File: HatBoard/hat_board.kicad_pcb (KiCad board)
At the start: 4 copper layers, 144 x 78 mm, 108 parts, among them J1 Molex FC Connection, J11 Molex FC Connection, J12 DF11 FC Connection, J17 Molex FC Connection, J18 DF11 FC Connection, J2 DF11 FC Connection, J23 Molex FC Connection, J24 DF11 FC Connection, J29 Molex FC Connection, J30 DF11 FC Connection, J35 Molex FC Connection, J36 DF11 FC Connection, SW1 SW_SPDT_321, SW2 SW_SPDT_321, SW3 SW_SPDT_321, SW4 SW_SPDT_321, SW5 SW_SPDT_321, SW6 SW_SPDT_321, U1 VEML7700, U10 VEML7700, U11 MCP9808_DFN, U12 DRV2605LDGS, U13 TCA4311A, U14 VEML7700, U15 MCP9808_DFN, U16 DRV2605LDGS, U17 TCA4311A, U18 VEML7700, U19 MCP9808_DFN, U2 DRV2605LDGS, U20 DRV2605LDGS, U21 TCA4311A, U22 VEML7700, U23 MCP9808_DFN, U24 DRV2605LDGS, U3 MCP9808_DFN, U4 TCA4311A, U5 TCA4311A, U6 VEML7700, U7 MCP9808_DFN, U8 DRV2605LDGS, U9 TCA4311A

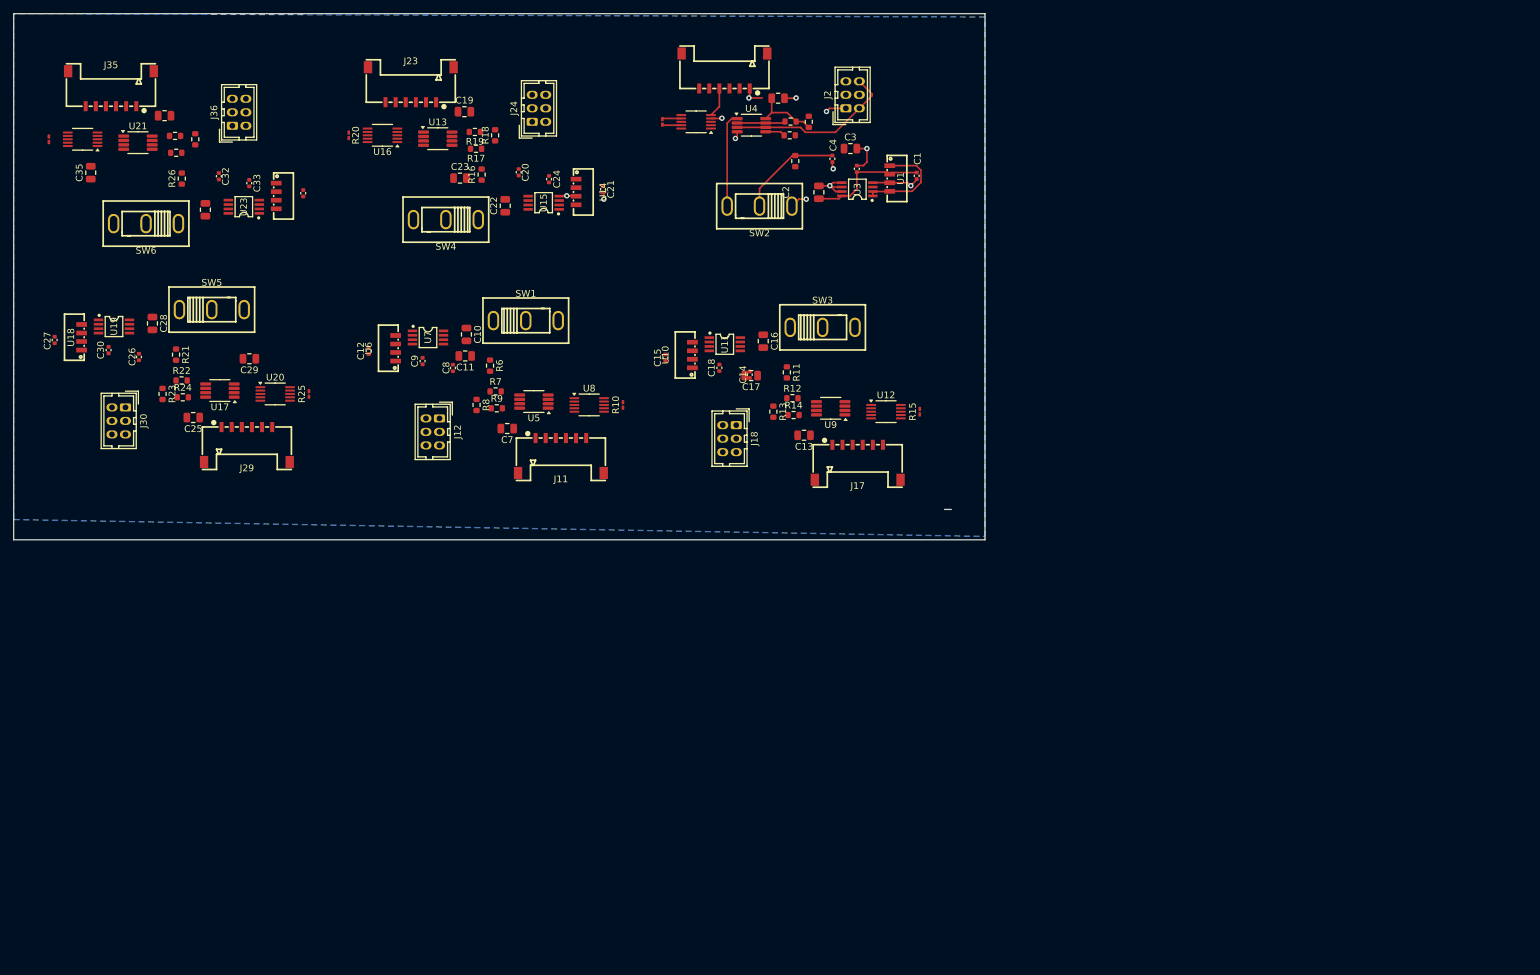
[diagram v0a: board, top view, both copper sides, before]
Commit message: placement with new temp sensor
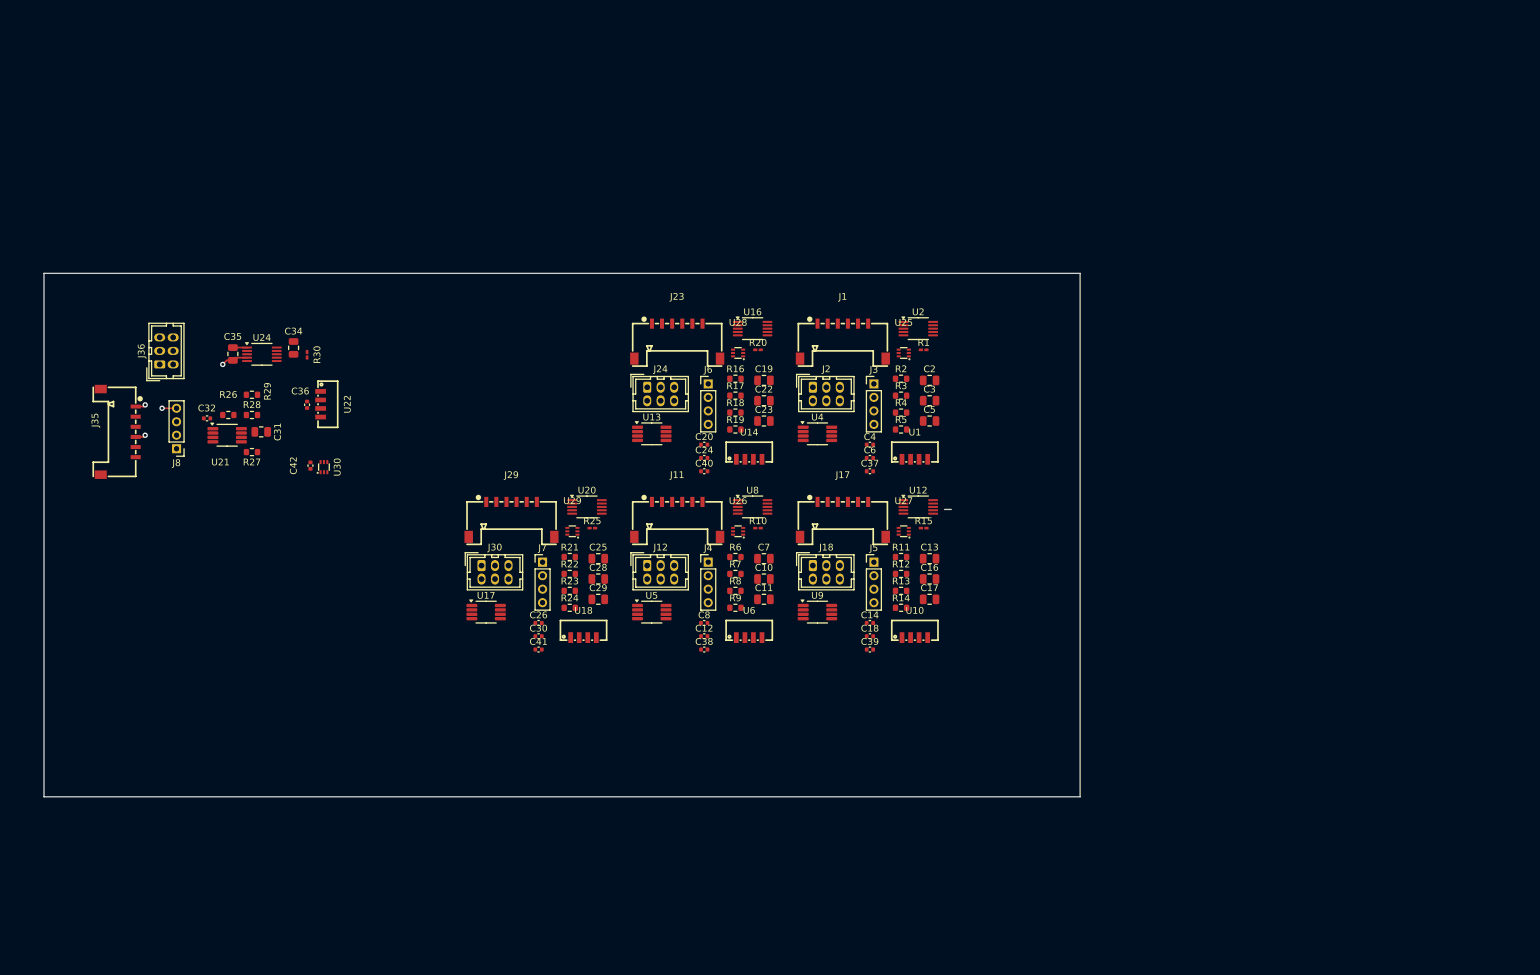
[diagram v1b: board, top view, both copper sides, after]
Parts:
- removed C1, C15, C21, C27, C33, C9: 100nF, Capacitor_SMD:C_0402_1005Metric
- removed SW1, SW2, SW3, SW4, SW5, SW6: SW_SPDT_321, easyeda2kicad:SW-TH_3P-P4.80-HX-SS12D10G4
- removed U11, U15, U19, U23, U3, U7: MCP9808_DFN, easyeda2kicad:MSOP-8_L3.0-W3.0-P0.65-LS4.9-BL
- added C37: 10nF, Capacitor_SMD:C_0402_1005Metric, F.Cu at (159.4, 93.8)
- added C38: 10nF, Capacitor_SMD:C_0402_1005Metric, F.Cu at (134.9, 120.3)
- added C39: 10nF, Capacitor_SMD:C_0402_1005Metric, F.Cu at (159.4, 120.3)
- added C40: 10nF, Capacitor_SMD:C_0402_1005Metric, F.Cu at (134.9, 93.8)
- added C41: 10nF, Capacitor_SMD:C_0402_1005Metric, F.Cu at (110.3, 120.3)
- added C42: 10nF, Capacitor_SMD:C_0402_1005Metric, F.Cu at (76.5, 93.0)
- added J3: Conn_01x04, Connector_PinHeader_2.00mm:PinHeader_1x04_P2.00mm_Vertical, F.Cu at (160.0, 80.9)
- added J4: Conn_01x04, Connector_PinHeader_2.00mm:PinHeader_1x04_P2.00mm_Vertical, F.Cu at (135.5, 107.3)
- added J5: Conn_01x04, Connector_PinHeader_2.00mm:PinHeader_1x04_P2.00mm_Vertical, F.Cu at (160.0, 107.3)
- added J6: Conn_01x04, Connector_PinHeader_2.00mm:PinHeader_1x04_P2.00mm_Vertical, F.Cu at (135.5, 80.9)
- added J7: Conn_01x04, Connector_PinHeader_2.00mm:PinHeader_1x04_P2.00mm_Vertical, F.Cu at (110.9, 107.3)
- added J8: Conn_01x04, Connector_PinHeader_2.00mm:PinHeader_1x04_P2.00mm_Vertical, F.Cu at (56.6, 90.5)
- added U25: TMP112AIDRLR, easyeda2kicad:SOT-563_L1.6-W1.2-P0.50-LS1.6-BR, F.Cu at (164.5, 76.3)
- added U26: TMP112AIDRLR, easyeda2kicad:SOT-563_L1.6-W1.2-P0.50-LS1.6-BR, F.Cu at (139.9, 102.7)
- added U27: TMP112AIDRLR, easyeda2kicad:SOT-563_L1.6-W1.2-P0.50-LS1.6-BR, F.Cu at (164.5, 102.7)
- added U28: TMP112AIDRLR, easyeda2kicad:SOT-563_L1.6-W1.2-P0.50-LS1.6-BR, F.Cu at (139.9, 76.3)
- added U29: TMP112AIDRLR, easyeda2kicad:SOT-563_L1.6-W1.2-P0.50-LS1.6-BR, F.Cu at (115.3, 102.7)
- added U30: TMP112AIDRLR, easyeda2kicad:SOT-563_L1.6-W1.2-P0.50-LS1.6-BR, F.Cu at (78.5, 93.2)
- moved U18 86.7 mm to (117.0, 118.5), turned to 0 degrees
- moved C30 76.6 mm to (110.3, 118.3), turned to 0 degrees
- moved C28 76.2 mm to (119.2, 109.8), turned to 0 degrees
- moved C26 71.2 mm to (110.3, 116.3), turned to 0 degrees
- moved R20 68.5 mm to (142.8, 75.8), turned to 0 degrees
- moved U6 67.7 mm to (141.5, 118.5), turned to 0 degrees
- moved R23 67.1 mm to (114.9, 111.6), turned to 0 degrees
- moved R21 65.6 mm to (114.9, 106.5), turned to 0 degrees
- moved R24 65.3 mm to (114.9, 114.1)
- moved C12 65.3 mm to (134.9, 118.3), turned to 0 degrees
- moved R22 64.3 mm to (114.9, 109.1)
- moved C25 63.6 mm to (119.2, 106.8), turned to 0 degrees
- moved C29 62.8 mm to (119.2, 112.8), turned to 0 degrees
- moved U16 61.9 mm to (142.1, 72.7), turned to 0 degrees
- moved C19 59.7 mm to (143.7, 80.4)
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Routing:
- net GND: track 34.9 -> 7.68 mm, vias 12 -> 3
- net /Face Board/SCLIN: track 25.4 -> 0.00 mm
- net /Face Board/SCL: track 22.2 -> 0.00 mm
- net +3V3: track 22.3 -> 1.51 mm, vias 0 -> 1
- net Net-(SW2-B): track 15.4 -> 0.00 mm
- net Net-(SW2-A): track 14.1 -> 0.00 mm
- net Net-(U4-VCC): track 9.80 -> 0.00 mm
- net Net-(U4-READY): track 2.95 -> 0.00 mm
- net Net-(U2-OUT+): track 2.84 -> 0.00 mm
- net Net-(U2-OUT-): track 2.84 -> 0.00 mm
- net Net-(U24-REG): track 0.00 -> 2.10 mm
- added copper zone on In2.Cu, net +3V3
- added copper zone on In1.Cu, net GND
- removed copper zone on B.Cu, net GND
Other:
- board size 144 x 78 mm -> 153.6 x 77.6 mm

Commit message: finished connections one board, review before copy and clean?
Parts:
- moved J36 4.91 mm to (57.0, 74.0), turned to -90 degrees
- moved R29 1.01 mm to (67.7, 83.5)
- moved C36 0.50 mm to (75.5, 84.0)
- moved C42 0.50 mm to (77.0, 93.0)
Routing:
- net /Face Board5/SCL: track 0.00 -> 42.7 mm, vias 0 -> 1
- net /Face Board5/SCLIN: track 0.00 -> 32.6 mm, vias 0 -> 2
- net GND: track 7.68 -> 26.6 mm, vias 3 -> 14
- net Net-(U21-VCC): track 0.00 -> 12.4 mm, vias 0 -> 2
- net +3V3: track 1.51 -> 13.2 mm, vias 1 -> 9
- net Net-(U24-OUT-): track 0.00 -> 4.84 mm
- net Net-(U24-OUT+): track 0.00 -> 4.78 mm
- net Net-(U21-EN): track 0.00 -> 3.74 mm
- net Net-(U21-READY): track 0.00 -> 1.83 mm

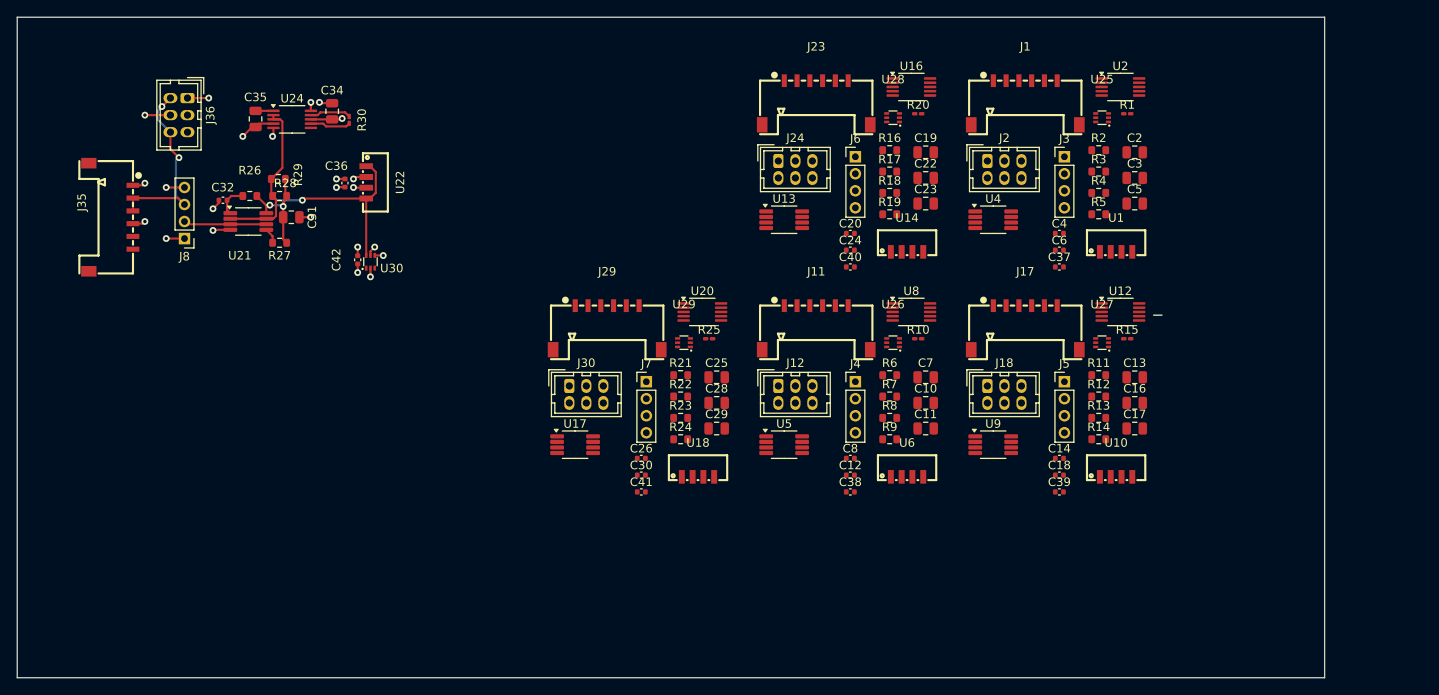
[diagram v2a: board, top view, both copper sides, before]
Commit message: no design errors faceboard
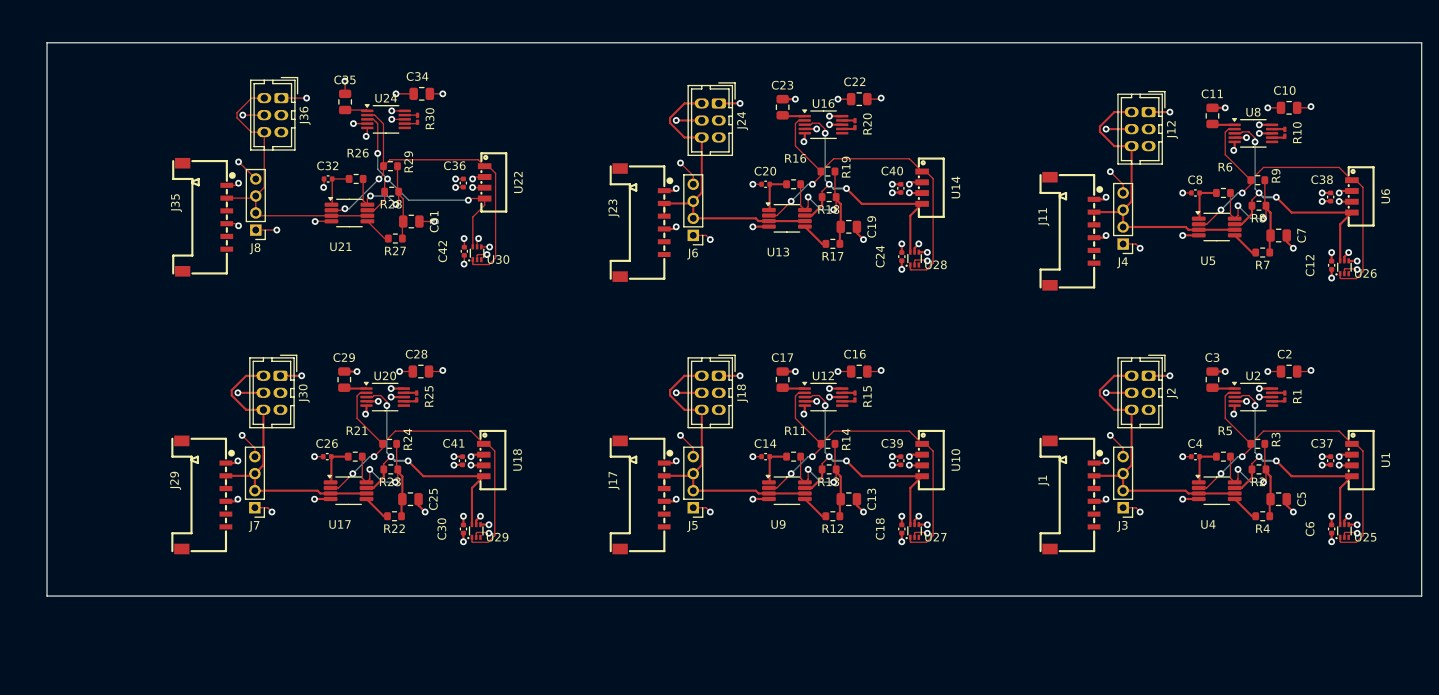
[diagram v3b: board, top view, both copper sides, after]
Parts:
- moved C38 66.2 mm to (191.3, 85.6), turned to -90 degrees
- moved U6 61.8 mm to (193.8, 85.5), turned to -90 degrees
- moved C12 61.7 mm to (191.4, 93.6), turned to -90 degrees
- moved U5 56.9 mm to (177.9, 89.1)
- moved U25 56.3 mm to (192.9, 124.9), turned to -90 degrees
- moved C10 55.0 mm to (186.4, 75.1)
- moved J12 54.1 mm to (169.9, 75.6), turned to -90 degrees
- moved U26 53.8 mm to (192.9, 93.9), turned to -90 degrees
- moved R9 52.9 mm to (182.8, 83.6), turned to 180 degrees
- moved J29 51.3 mm to (58.9, 120.6), turned to -90 degrees
- moved C8 51.2 mm to (175.4, 85.1), turned to 180 degrees
- moved R8 50.0 mm to (182.9, 86.6), turned to 180 degrees
- moved C11 49.8 mm to (177.4, 76.1), turned to 90 degrees
- moved R10 49.4 mm to (185.9, 78.1), turned to 90 degrees
- moved J17 49.1 mm to (110.4, 120.6), turned to -90 degrees
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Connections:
- R13 pad 2: /Face Board2/SCL -> /Face Board2/SDA
- R18 pad 2: /Face Board3/SCL -> /Face Board3/SDA
- R2 pad 2: /Face Board/SCL -> /Face Board/SDA
- R23 pad 2: /Face Board4/SCL -> /Face Board4/SDA
- R28 pad 2: /Face Board5/SCL -> /Face Board5/SDA
- R8 pad 2: /Face Board1/SCL -> /Face Board1/SDA
- U1 pad 4: /Face Board/SCL -> /Face Board/SDA
- U10 pad 4: /Face Board2/SCL -> /Face Board2/SDA
- U12 pad 3: /Face Board2/SCL -> /Face Board2/SDA
- U13 pad 7: /Face Board3/SCL -> /Face Board3/SDA
- U14 pad 4: /Face Board3/SCL -> /Face Board3/SDA
- U16 pad 3: /Face Board3/SCL -> /Face Board3/SDA
- U17 pad 7: /Face Board4/SCL -> /Face Board4/SDA
- U18 pad 4: /Face Board4/SCL -> /Face Board4/SDA
- U2 pad 3: /Face Board/SCL -> /Face Board/SDA
- U20 pad 3: /Face Board4/SCL -> /Face Board4/SDA
- U21 pad 7: /Face Board5/SCL -> /Face Board5/SDA
- U22 pad 4: /Face Board5/SCL -> /Face Board5/SDA
- U24 pad 3: /Face Board5/SCL -> /Face Board5/SDA
- U25 pad 6: /Face Board/SCL -> /Face Board/SDA
- U26 pad 6: /Face Board1/SCL -> /Face Board1/SDA
- U27 pad 6: /Face Board2/SCL -> /Face Board2/SDA
- U28 pad 6: /Face Board3/SCL -> /Face Board3/SDA
- U29 pad 6: /Face Board4/SCL -> /Face Board4/SDA
- U30 pad 6: /Face Board5/SCL -> /Face Board5/SDA
- U4 pad 7: /Face Board/SCL -> /Face Board/SDA
- U5 pad 7: /Face Board1/SCL -> /Face Board1/SDA
- U6 pad 4: /Face Board1/SCL -> /Face Board1/SDA
- U8 pad 3: /Face Board1/SCL -> /Face Board1/SDA
- U9 pad 7: /Face Board2/SCL -> /Face Board2/SDA
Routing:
- net GND: track 26.6 -> 161.2 mm, vias 14 -> 96
- net +3V3: track 13.2 -> 81.8 mm, vias 9 -> 54
- net /Face Board1/SCL: track 0.00 -> 44.9 mm, vias 0 -> 2
- net /Face Board4/SCL: track 0.00 -> 44.9 mm, vias 0 -> 2
- net /Face Board/SCL: track 0.00 -> 44.9 mm, vias 0 -> 2
- net /Face Board3/SCL: track 0.00 -> 44.9 mm, vias 0 -> 2
- net /Face Board2/SCL: track 0.00 -> 44.9 mm, vias 0 -> 2
- net /Face Board1/SCLIN: track 0.00 -> 37.9 mm
- net /Face Board/SCLIN: track 0.00 -> 37.9 mm
- net /Face Board4/SCLIN: track 0.00 -> 37.9 mm
- net /Face Board3/SCLIN: track 0.00 -> 37.9 mm
- net /Face Board2/SCLIN: track 0.00 -> 37.9 mm
- net /Face Board4/SDA: track 0.00 -> 33.5 mm, vias 0 -> 3
- net /Face Board3/SDA: track 0.00 -> 33.5 mm, vias 0 -> 3
- net /Face Board2/SDA: track 0.00 -> 33.5 mm, vias 0 -> 3
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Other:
- board size 153.6 x 77.6 mm -> 161.5 x 65 mm
